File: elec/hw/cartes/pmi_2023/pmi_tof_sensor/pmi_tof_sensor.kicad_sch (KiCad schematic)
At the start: 31 parts, among them J1 tof_sensor_female, Q1 BSS84, Q4 BSS8402DW-7-F, U3 VL53L1CXV0FY1, U4 VL53L5CXV0GC

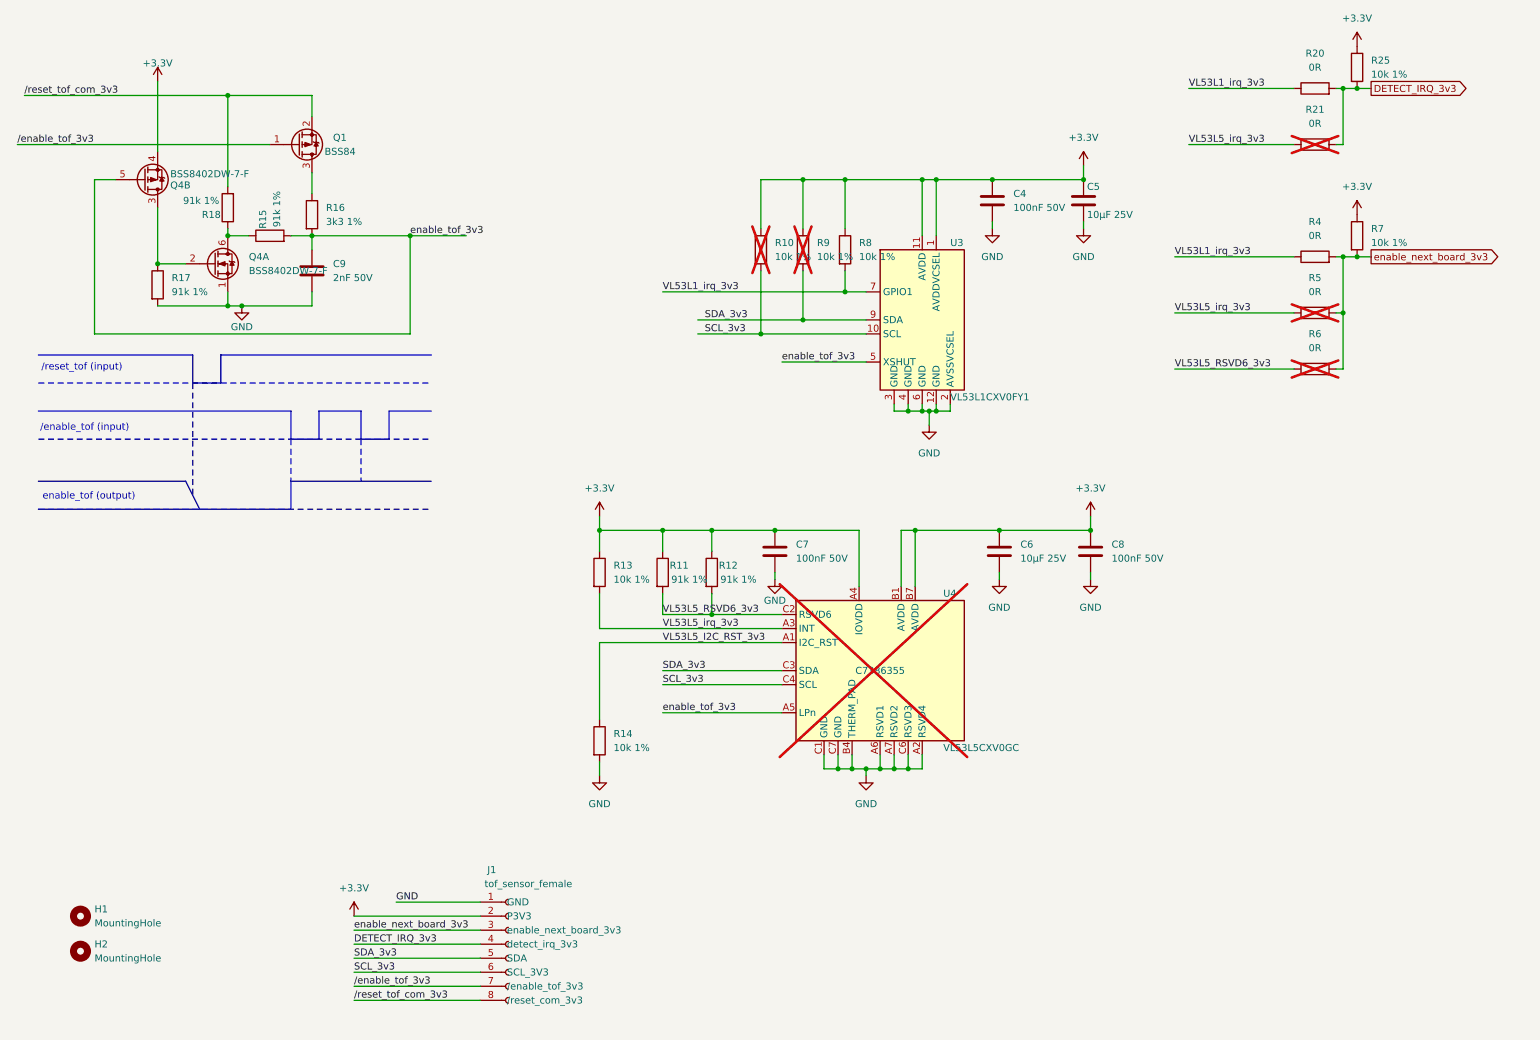
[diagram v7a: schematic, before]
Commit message: tof_sensor : changed not monted components to match new pmi project: L5 mounted and L1 not mounted
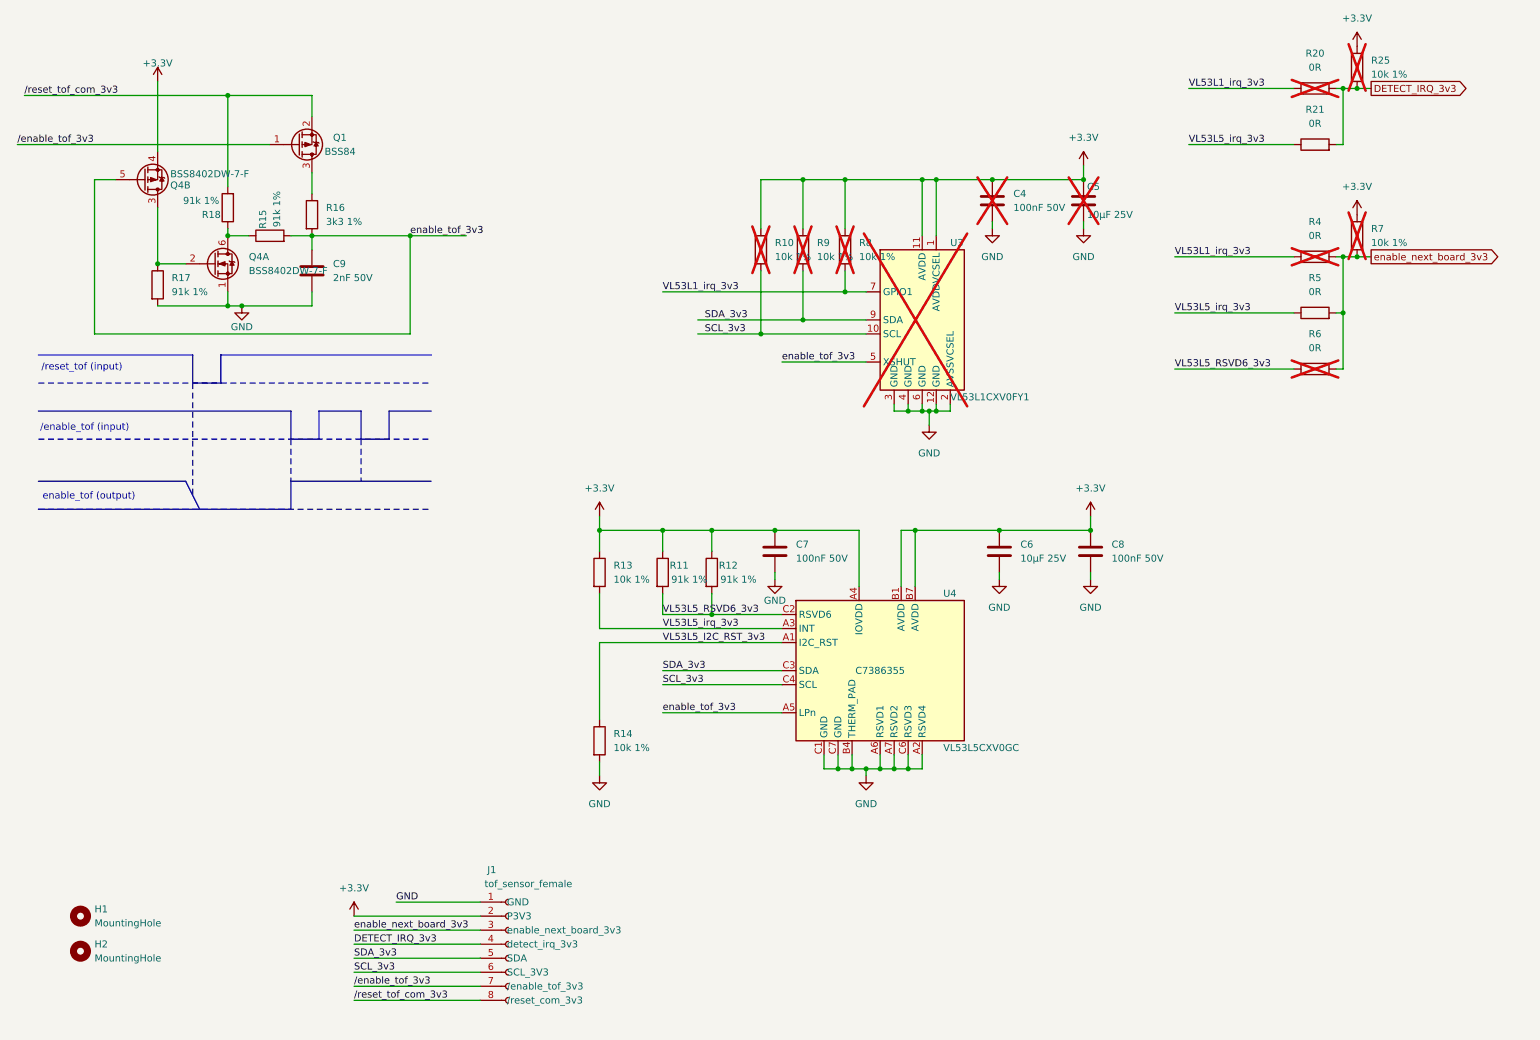
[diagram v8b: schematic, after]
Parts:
- C4, C5, R20, R25, R4, R7, R8, U3: now not fitted
- R21, R5, U4: now fitted
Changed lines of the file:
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@@
 (kicad_sch
-	(version 20231120)
+	(version 20250114)
 	(generator "eeschema")
-	(generator_version "8.0")
+	(generator_version "9.0")
 	(paper "A4")
+	(text "/enable_tof (input)"
+		(exclude_from_sim no)
+		(at 26.162 89.408 0)
+		(effects
+			(font
+				(size 1.27 1.27)
+			)
+		)
+	)
+	(text "/reset_tof (input)"
+		(exclude_from_sim no)
+		(at 25.654 78.486 0)
+		(effects
+			(font
+				(size 1.27 1.27)
+			)
+		)
+	)
+	(text "enable_tof (output)"
+		(exclude_from_sim no)
+		(at 26.924 101.854 0)
+		(effects
+			(font
+				(size 1.27 1.27)
+			)
+		)
+	)
 	(junction
 		(at 54.61 67.31)
@@
 		)
 	)
-	(text "/enable_tof (input)"
-		(exclude_from_sim no)
-		(at 26.162 89.408 0)
-		(effects
-			(font
-				(size 1.27 1.27)
-			)
-		)
-	)
-	(text "/reset_tof (input)"
-		(exclude_from_sim no)
-		(at 25.654 78.486 0)
-		(effects
-			(font
-				(size 1.27 1.27)
-			)
-		)
-	)
-	(text "enable_tof (output)"
-		(exclude_from_sim no)
-		(at 26.924 101.854 0)
-		(effects
-			(font
-				(size 1.27 1.27)
-			)
-		)
-	)
 	(label "enable_next_board_3v3"
 		(at 74.93 180.34 0)
-		(fields_autoplaced yes)
 		(effects
 			(font
@@
 	(label "VL53L5_irq_3v3"
 		(at 226.06 38.1 0)
-		(fields_autoplaced yes)
 		(effects
 			(font
@@
 	(label "DETECT_IRQ_3v3"
 		(at 74.93 182.88 0)
-		(fields_autoplaced yes)
 		(effects
 			(font
@@
 	(label "VL53L5_RSVD6_3v3"
 		(at 130.81 123.19 0)
-		(fields_autoplaced yes)
 		(effects
 			(font
@@
 	(label "VL53L5_I2C_RST_3v3"
 		(at 130.81 128.27 0)
-		(fields_autoplaced yes)
 		(effects
 			(font
@@
 	(label "SDA_3v3"
 		(at 138.43 69.85 0)
-		(fields_autoplaced yes)
 		(effects
 			(font
@@
 	(label "SDA_3v3"
 		(at 74.93 185.42 0)
-		(fields_autoplaced yes)
 		(effects
 			(font
@@
 	(label "{slash}enable_tof_3v3"
 		(at 13.97 38.1 0)
-		(fields_autoplaced yes)
 		(effects
 			(font
@@
 	(label "SCL_3v3"
 		(at 130.81 135.89 0)
-		(fields_autoplaced yes)
 		(effects
 			(font
@@
 	(label "VL53L5_irq_3v3"
 		(at 223.52 68.58 0)
-		(fields_autoplaced yes)
 		(effects
 			(font
@@
 	(label "SCL_3v3"
 		(at 138.43 72.39 0)
-		(fields_autoplaced yes)
 		(effects
 			(font
@@
 	(label "VL53L1_irq_3v3"
 		(at 226.06 27.94 0)
-		(fields_autoplaced yes)
 		(effects
 			(font
@@
 	(label "GND"
 		(at 82.55 175.26 0)
-		(fields_autoplaced yes)
 		(effects
 			(font
@@
 	(label "enable_tof_3v3"
 		(at 130.81 140.97 0)
-		(fields_autoplaced yes)
 		(effects
 			(font
@@
 	(label "SCL_3v3"
 		(at 74.93 187.96 0)
-		(fields_autoplaced yes)
 		(effects
 			(font
@@
 	(label "enable_tof_3v3"
 		(at 85.09 54.61 0)
-		(fields_autoplaced yes)
 		(effects
 			(font
@@
 	(label "{slash}reset_tof_com_3v3"
 		(at 15.24 29.21 0)
-		(fields_autoplaced yes)
 		(effects
 			(font
@@
 	(label "SDA_3v3"
 		(at 130.81 133.35 0)
-		(fields_autoplaced yes)
 		(effects
 			(font
@@
 	(label "VL53L5_irq_3v3"
 		(at 130.81 125.73 0)
-		(fields_autoplaced yes)
 		(effects
 			(font
@@
 	(label "enable_tof_3v3"
 		(at 152.4 77.47 0)
-		(fields_autoplaced yes)
 		(effects
 			(font
@@
 	(label "{slash}enable_tof_3v3"
 		(at 74.93 190.5 0)
-		(fields_autoplaced yes)
 		(effects
 			(font
@@
 	(label "VL53L5_RSVD6_3v3"
 		(at 223.52 78.74 0)
-		(fields_autoplaced yes)
 		(effects
 			(font
@@
 	(label "{slash}reset_tof_com_3v3"
 		(at 74.93 193.04 0)
-		(fields_autoplaced yes)
 		(effects
 			(font
@@
 	(label "VL53L1_irq_3v3"
 		(at 130.81 64.77 0)
-		(fields_autoplaced yes)
 		(effects
 			(font
@@
 	(label "VL53L1_irq_3v3"
 		(at 223.52 58.42 0)
-		(fields_autoplaced yes)
 		(effects
 			(font
@@
 		(in_bom yes)
 		(on_board yes)
-		(dnp no)
+		(dnp yes)
 		(fields_autoplaced yes)
 		(property "Reference" "C4"
@@
 		(in_bom yes)
 		(on_board yes)
-		(dnp yes)
+		(dnp no)
 		(fields_autoplaced yes)
 		(property "Reference" "R21"
@@
 		(in_bom yes)
 		(on_board yes)
-		(dnp no)
+		(dnp yes)
 		(property "Reference" "C5"
 			(at 207.645 45.72 0)
@@
 		(in_bom yes)
 		(on_board yes)
-		(dnp no)
+		(dnp yes)
 		(fields_autoplaced yes)
 		(property "Reference" "R7"
@@
 		(in_bom yes)
 		(on_board yes)
-		(dnp yes)
+		(dnp no)
 		(fields_autoplaced yes)
 		(property "Reference" "R5"
@@
 		(in_bom yes)
 		(on_board yes)
-		(dnp no)
+		(dnp yes)
 		(fields_autoplaced yes)
 		(property "Reference" "R4"
@@
 		(in_bom yes)
 		(on_board yes)
-		(dnp no)
+		(dnp yes)
 		(property "Reference" "U3"
 			(at 182.88 55.88 0)
@@
 		(in_bom yes)
 		(on_board yes)
-		(dnp no)
+		(dnp yes)
 		(fields_autoplaced yes)
 		(property "Reference" "R8"
@@
 		(in_bom yes)
 		(on_board yes)
-		(dnp yes)
+		(dnp no)
 		(property "Reference" "U4"
 			(at 181.61 119.38 0)
@@
 		(in_bom yes)
 		(on_board yes)
-		(dnp no)
+		(dnp yes)
 		(fields_autoplaced yes)
 		(property "Reference" "R25"
@@
 		(in_bom yes)
 		(on_board yes)
-		(dnp no)
+		(dnp yes)
 		(fields_autoplaced yes)
 		(property "Reference" "R20"
@@
 		)
 	)
+	(embedded_fonts no)
 )
